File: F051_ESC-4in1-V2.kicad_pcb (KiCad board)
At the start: 4 copper layers, 46 x 55.8 mm, 222 parts, among them J1 Conn_01x02, J11 Conn_01x03, J14 Conn_01x03, J2 Conn_01x10, J3 Conn_01x05, J4 Conn_01x05, J5 Conn_01x05, J6 Conn_01x03, J7 Conn_01x05, J8 Conn_01x03, J9 Conn_01x10, Q1 TPHR8504PL, Q10 TPHR8504PL, Q11 TPHR8504PL, Q12 TPHR8504PL, Q13 TPHR8504PL, Q14 TPHR8504PL, Q15 TPHR8504PL, Q16 TPHR8504PL, Q17 TPHR8504PL, Q18 TPHR8504PL, Q19 TPHR8504PL, Q2 TPHR8504PL, Q20 TPHR8504PL, Q21 TPHR8504PL, Q22 TPHR8504PL, Q23 TPHR8504PL, Q24 TPHR8504PL, Q3 TPHR8504PL, Q4 TPHR8504PL, Q5 TPHR8504PL, Q6 TPHR8504PL, Q7 TPHR8504PL, Q8 TPHR8504PL, Q9 TPHR8504PL, U1 STM32F051K6Ux, U10 FD6288Q, U11 STM32F051K6Ux, U12 FD6288Q, U13 L78L12_SOT89, U14 MP4560_QFN10, U2 FD6288Q, U3 L78L12_SOT89, U4 LP2985-3.3, U5 INA139, U6 FD6288Q, U7 OPA340NA, U8 STM32F051K6Ux, U9 STM32F051K6Ux

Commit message: More routing
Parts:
- moved C17 54.9 mm to (132.9, 101.1)
- moved C20 54.9 mm to (132.9, 98.8)
- moved C50 54.9 mm to (132.9, 87.3)
- moved C52 54.9 mm to (132.9, 78.2)
- moved C53 54.9 mm to (132.9, 94.2)
- moved C54 54.9 mm to (132.9, 85.1)
- moved C55 54.9 mm to (132.9, 75.9)
- moved C56 54.9 mm to (132.9, 91.9)
- moved C57 54.9 mm to (132.9, 82.8)
- moved C59 54.9 mm to (132.9, 80.5)
- moved C61 54.9 mm to (132.9, 96.5)
- moved C63 54.9 mm to (132.9, 89.6)
- moved C16 28.6 mm to (147.1, 89.6)
- moved C18 28.6 mm to (147.1, 82.8)
- moved C19 28.6 mm to (147.1, 91.9)
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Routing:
- net Net-(Q4-Pad4): track 15.9 -> 0.00 mm
- net Net-(Q22-Pad4): track 15.1 -> 0.00 mm
- net /MCU 3/PhaseA: track 17.6 -> 2.95 mm, vias 30 -> 28
- net /MCU 4/PhaseC: track 19.6 -> 5.28 mm, vias 29 -> 27
- net /MCU 1/PhaseA: track 18.8 -> 5.94 mm, vias 29 -> 27
- net /MCU 3/PhaseB: track 15.5 -> 2.76 mm, vias 29 -> 27
- net Net-(Q16-Pad4): track 0.00 -> 11.2 mm
- net /MCU 1/PhaseB: track 15.1 -> 4.30 mm, vias 29 -> 27
- net Net-(Q14-Pad4): track 0.00 -> 10.6 mm
- net Net-(Q24-Pad4): track 9.34 -> 0.00 mm
- net /MOSFET Driver 3/HO1: track 8.67 -> 0.02 mm
- net /MOSFET Driver 3/HO2: track 7.22 -> 0.00 mm
- net /MCU 4/PhaseB: track 11.5 -> 4.43 mm, vias 29 -> 28
- net VCC_Shunt: track 6.57 -> 0.00 mm, vias 234 -> 107
- net /MOSFET Driver 3/VB2: track 7.54 -> 1.61 mm
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- added copper zone on F.Cu, net +5V
- added copper zone on F.Cu, net Net-(C70-Pad1)

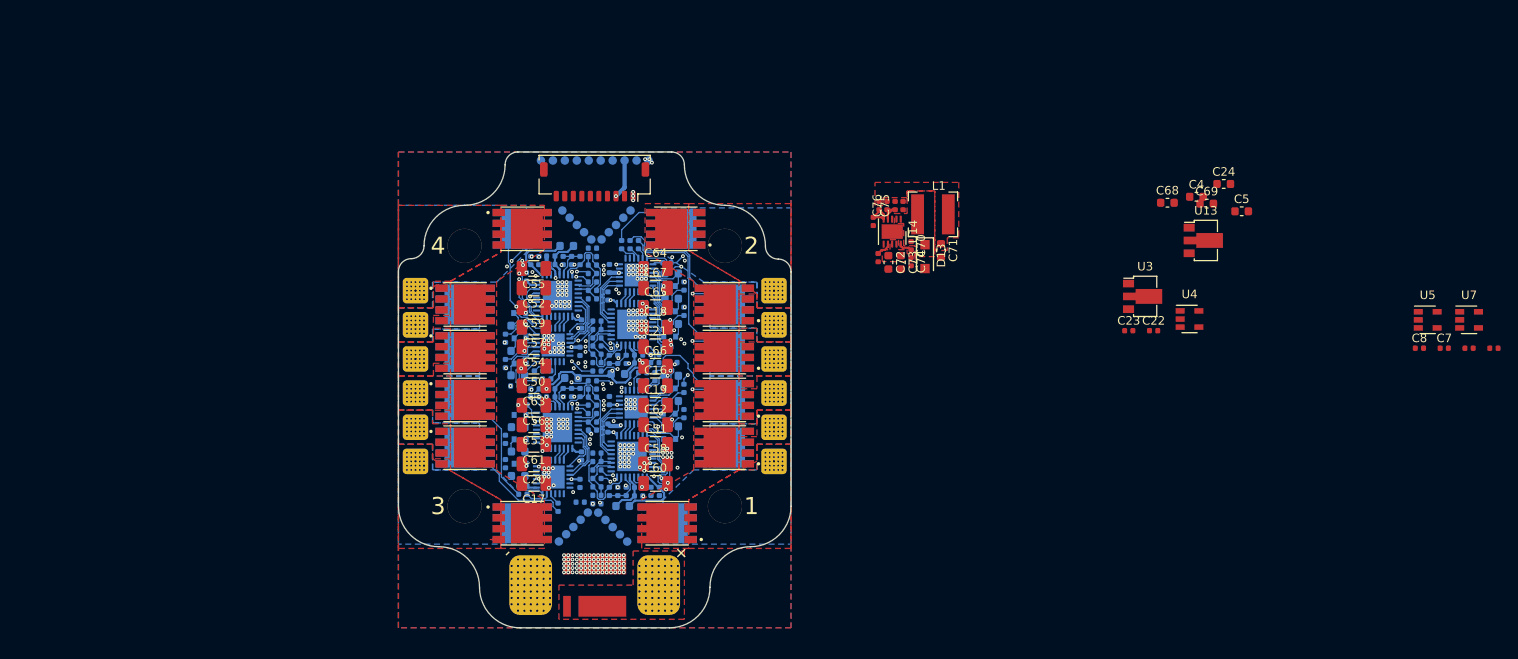
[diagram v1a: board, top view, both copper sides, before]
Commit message: Lots of changes made with back being rerouted
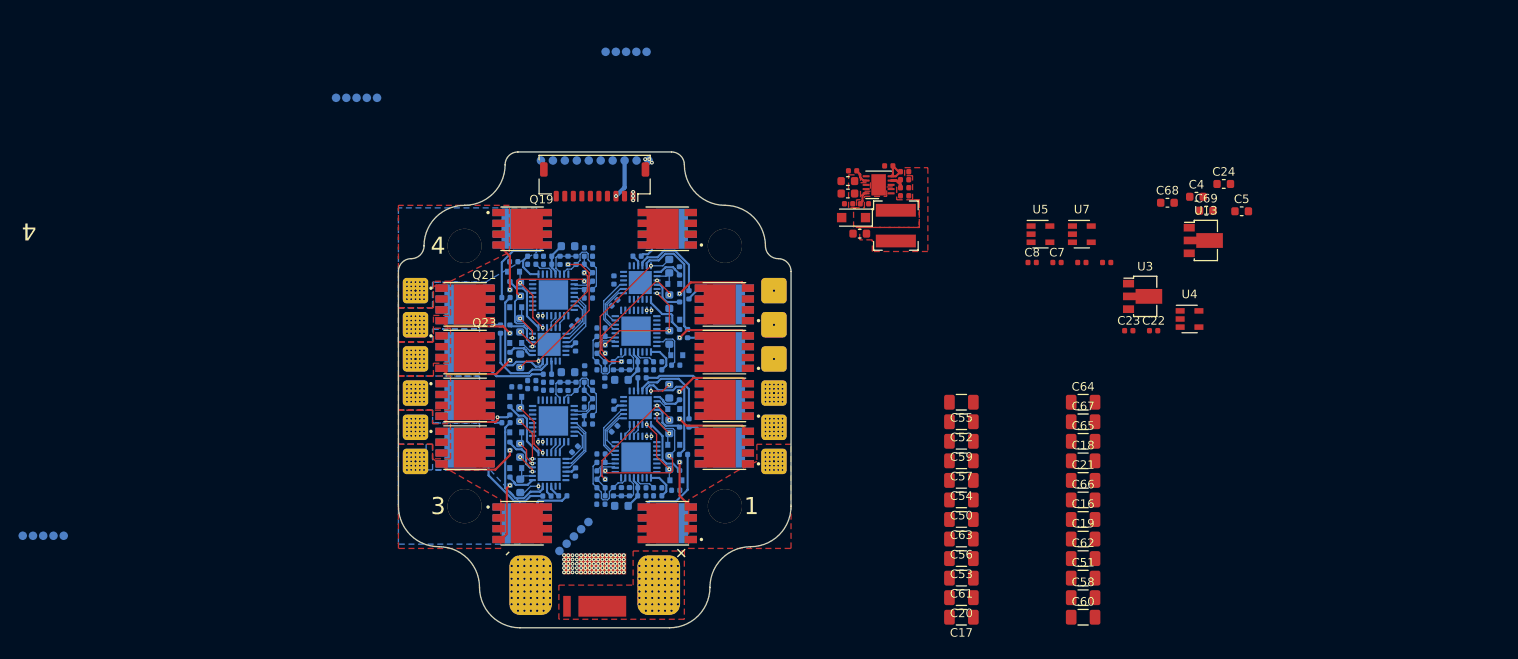
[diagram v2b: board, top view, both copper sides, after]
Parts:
- removed J14: Conn_01x03, Connector_Wire:Conn_MotorPhase
- added J10: Conn_01x03, Connector_Wire:Conn_MotorPhase, B.Cu at (119.0, 82.5)
- C1, C27, C41: value 10nF -> 0.1uF
- C10: value 0.1uF -> 1uF; footprint Capacitor_SMD:C_0603_1608Metric -> Capacitor_SMD:C_0402_1005Metric
- C11, C45, C9: value 0.1uF -> 10nF
- C12, C46: value 0.1uF -> 1uF
- C13, C14, C15, C25, C26, C47, C48, C49: footprint Capacitor_SMD:C_0603_1608Metric -> Capacitor_SMD:C_0402_1005Metric
- C2, C42: value 1uF -> 0.1uF; footprint Capacitor_SMD:C_0402_1005Metric -> Capacitor_SMD:C_0603_1608Metric
- C28: value 1uF -> 0.1uF
- C29, C3, C30, C31, C43, C44, C6: footprint Capacitor_SMD:C_0402_1005Metric -> Capacitor_SMD:C_0603_1608Metric
- J6, J8: moved to B.Cu
- Q1, Q10, Q11, Q12, Q13, Q14, Q15, Q16, Q17, Q18, Q19, Q2, Q20, Q21, Q22, Q23, Q24, Q3, Q4, Q5, Q6, Q7, Q8, Q9: value TPHR8504PL -> TPH1R204PB; footprint Footprints:TPHR8504PL -> Footprints:TPH1R204PB
- R10, R12, R32, R33, R55, R56, R57, R58, R60, R7, R8, R9: value 10k -> 10
- R11, R34, R35, R36, R37, R59: value 1k -> 10
- R14, R16, R17, R62, R63, R64: value 1k -> 10k
- R18, R19, R22, R26, R4, R5, R6, R66, R67: value 10 -> 10k
- R20, R21, R23, R24, R25, R68, R69, R70, R71: value 10 -> 1k
- R28, R29, R30: value 10k -> 1k
- U1, U11, U8: value STM32F051K6Ux -> FD6288Q; footprint Package_DFN_QFN:QFN-32-1EP_5x5mm_P0.5mm_EP3.45x3.45mm -> Package_DFN_QFN:QFN-24-1EP_4x4mm_P0.5mm_EP2.7x2.7mm
- U12, U2, U6: value FD6288Q -> STM32F051K6Ux; footprint Package_DFN_QFN:QFN-24-1EP_4x4mm_P0.5mm_EP2.7x2.7mm -> Package_DFN_QFN:QFN-32-1EP_5x5mm_P0.5mm_EP3.45x3.45mm
- moved J5 76.4 mm to (75.4, 107.2), turned to 0 degrees
- moved J3 55.7 mm to (143.7, 50.5), turned to 0 degrees
- moved C16 52.5 mm to (197.2, 105.3)
- moved C17 52.5 mm to (183.0, 116.8)
- moved C18 52.5 mm to (197.2, 98.4)
- moved C20 52.5 mm to (183.0, 114.5)
- moved C21 52.5 mm to (197.2, 100.7)
- moved C50 52.5 mm to (183.0, 103.0)
- moved C51 52.5 mm to (197.2, 112.2)
- moved C52 52.5 mm to (183.0, 93.9)
- moved C53 52.5 mm to (183.0, 109.9)
- moved C54 52.5 mm to (183.0, 100.7)
- moved C57 52.5 mm to (183.0, 98.4)
- moved C58 52.5 mm to (197.2, 114.5)
- moved C59 52.5 mm to (183.0, 96.2)
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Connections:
- C1 pad 1: +3.3VA_1 -> +12V_2
- C10 pad 1: /MOSFET Driver 2/VB1 -> +3.3VA_2
- C10 pad 2: /MCU 2/PhaseA -> GND
- C11 pad 1: /MCU 1/NRST -> +3.3VA_1
- C12 pad 1: +12V_2 -> +3.3VA_1
- C13 pad 1: /MOSFET Driver 1/VB1 -> +3V3
- C13 pad 2: /MCU 1/PhaseA -> GND
- C14 pad 1: /MOSFET Driver 1/VB2 -> +3V3
- C14 pad 2: /MCU 1/PhaseB -> GND
- C15 pad 1: /MOSFET Driver 1/VB3 -> /MCU_1/NRST
- C15 pad 2: /MCU 1/PhaseC -> GND
- C2 pad 1: +3.3VA_1 -> /MOSFET_Driver_1/VB1
- C2 pad 2: GND -> /MCU_1/PhaseA
- C25 pad 1: /MOSFET Driver 2/VB2 -> +3V3
- C25 pad 2: /MCU 2/PhaseB -> GND
- C26 pad 1: /MOSFET Driver 2/VB3 -> +3V3
- C26 pad 2: /MCU 2/PhaseC -> GND
- C27 pad 1: +3.3VA_2 -> /MCU_2/NRST
- C28 pad 1: +3.3VA_2 -> +12V_2
- C29 pad 1: +3V3 -> /MOSFET_Driver_2/VB1
- C29 pad 2: GND -> /MCU_2/PhaseA
- C3 pad 1: +3V3 -> /MOSFET_Driver_1/VB2
- C3 pad 2: GND -> /MCU_1/PhaseB
- C30 pad 1: +3V3 -> /MOSFET_Driver_2/VB2
- C30 pad 2: GND -> /MCU_2/PhaseB
- C31 pad 1: /MCU 2/NRST -> /MOSFET_Driver_2/VB3
- C31 pad 2: GND -> /MCU_2/PhaseC
- C41 pad 1: +3.3VA_4 -> +12V_1
- C42 pad 1: +3.3VA_4 -> /MOSFET_Driver_4/VB1
- C42 pad 2: GND -> /MCU_4/PhaseA
- C43 pad 1: +3V3 -> /MOSFET_Driver_4/VB2
- C43 pad 2: GND -> /MCU_4/PhaseB
- C44 pad 1: +3V3 -> /MOSFET_Driver_4/VB3
- C44 pad 2: GND -> /MCU_4/PhaseC
- C45 pad 1: /MCU 4/NRST -> +3.3VA_4
- C46 pad 1: +12V_1 -> +3.3VA_4
- C47 pad 1: /MOSFET Driver 4/VB1 -> +3V3
- C47 pad 2: /MCU 4/PhaseA -> GND
- C48 pad 1: /MOSFET Driver 4/VB2 -> +3V3
- C48 pad 2: /MCU 4/PhaseB -> GND
- C49 pad 1: /MOSFET Driver 4/VB3 -> /MCU_4/NRST
- C49 pad 2: /MCU 4/PhaseC -> GND
- C6 pad 1: +3V3 -> /MOSFET_Driver_1/VB3
- C6 pad 2: GND -> /MCU_1/PhaseC
- C9 pad 1: +12V_2 -> +3.3VA_2
- D1 pad 1: /MOSFET Driver 2/VB1 -> /MOSFET_Driver_2/VB1
- D10 pad 1: /MOSFET Driver 4/VB1 -> /MOSFET_Driver_4/VB1
- D11 pad 1: /MOSFET Driver 4/VB2 -> /MOSFET_Driver_4/VB2
- D12 pad 1: /MOSFET Driver 4/VB3 -> /MOSFET_Driver_4/VB3
- D2 pad 1: /MOSFET Driver 1/VB1 -> /MOSFET_Driver_1/VB1
- D3 pad 1: /MOSFET Driver 1/VB2 -> /MOSFET_Driver_1/VB2
- D4 pad 1: /MOSFET Driver 1/VB3 -> /MOSFET_Driver_1/VB3
- D5 pad 1: /MOSFET Driver 2/VB2 -> /MOSFET_Driver_2/VB2
- D6 pad 1: /MOSFET Driver 2/VB3 -> /MOSFET_Driver_2/VB3
- J3 pad 1: /MCU 1/SWCLK -> /MCU_1/SWCLK
- J3 pad 2: /MCU 1/SWDIO -> /MCU_1/SWDIO
- J3 pad 3: /MCU 1/NRST -> /MCU_1/NRST
- J3 pad 4: /MCU 1/USART1_RX -> /MCU_1/USART1_RX
- J3 pad 5: /MCU 1/USART1_TX -> /MCU_1/USART1_TX
- J5 pad 1: /MCU 2/SWCLK -> /MCU_2/SWCLK
- J5 pad 2: /MCU 2/SWDIO -> /MCU_2/SWDIO
- J5 pad 3: /MCU 2/NRST -> /MCU_2/NRST
- J5 pad 4: /MCU 2/USART1_RX -> /MCU_2/USART1_RX
- J5 pad 5: /MCU 2/USART1_TX -> /MCU_2/USART1_TX
- J6 pad 1: /MCU 1/PhaseC -> /MCU_1/PhaseC
- J6 pad 2: /MCU 1/PhaseB -> /MCU_1/PhaseB
- J6 pad 3: /MCU 1/PhaseA -> /MCU_1/PhaseA
- J7 pad 1: /MCU 4/SWCLK -> /MCU_4/SWCLK
- J7 pad 2: /MCU 4/SWDIO -> /MCU_4/SWDIO
- J7 pad 3: /MCU 4/NRST -> /MCU_4/NRST
- J7 pad 4: /MCU 4/USART1_RX -> /MCU_4/USART1_RX
- J7 pad 5: /MCU 4/USART1_TX -> /MCU_4/USART1_TX
- J8 pad 1: /MCU 2/PhaseC -> /MCU_2/PhaseC
- J8 pad 2: /MCU 2/PhaseB -> /MCU_2/PhaseB
- J8 pad 3: /MCU 2/PhaseA -> /MCU_2/PhaseA
- Q1 pad 1: /MCU 1/PhaseA -> /MCU_1/PhaseA
- Q1 pad 2: /MCU 1/PhaseA -> /MCU_1/PhaseA
- Q1 pad 3: /MCU 1/PhaseA -> /MCU_1/PhaseA
- Q10 pad 5: /MCU 2/PhaseB -> /MCU_2/PhaseB
- Q10 pad 6: /MCU 2/PhaseB -> /MCU_2/PhaseB
- Q10 pad 7: /MCU 2/PhaseB -> /MCU_2/PhaseB
- Q10 pad 8: /MCU 2/PhaseB -> /MCU_2/PhaseB
- Q10 pad 9: /MCU 2/PhaseB -> /MCU_2/PhaseB
- Q11 pad 1: /MCU 2/PhaseC -> /MCU_2/PhaseC
- Q11 pad 2: /MCU 2/PhaseC -> /MCU_2/PhaseC
- Q11 pad 3: /MCU 2/PhaseC -> /MCU_2/PhaseC
- Q12 pad 5: /MCU 2/PhaseC -> /MCU_2/PhaseC
- Q12 pad 6: /MCU 2/PhaseC -> /MCU_2/PhaseC
- Q12 pad 7: /MCU 2/PhaseC -> /MCU_2/PhaseC
- Q12 pad 8: /MCU 2/PhaseC -> /MCU_2/PhaseC
- Q12 pad 9: /MCU 2/PhaseC -> /MCU_2/PhaseC
- Q19 pad 1: /MCU 4/PhaseA -> /MCU_4/PhaseA
- Q19 pad 2: /MCU 4/PhaseA -> /MCU_4/PhaseA
- Q19 pad 3: /MCU 4/PhaseA -> /MCU_4/PhaseA
- Q2 pad 5: /MCU 1/PhaseA -> /MCU_1/PhaseA
- Q2 pad 6: /MCU 1/PhaseA -> /MCU_1/PhaseA
- Q2 pad 7: /MCU 1/PhaseA -> /MCU_1/PhaseA
- Q2 pad 8: /MCU 1/PhaseA -> /MCU_1/PhaseA
- Q2 pad 9: /MCU 1/PhaseA -> /MCU_1/PhaseA
- Q20 pad 5: /MCU 4/PhaseA -> /MCU_4/PhaseA
- Q20 pad 6: /MCU 4/PhaseA -> /MCU_4/PhaseA
- Q20 pad 7: /MCU 4/PhaseA -> /MCU_4/PhaseA
- Q20 pad 8: /MCU 4/PhaseA -> /MCU_4/PhaseA
- Q20 pad 9: /MCU 4/PhaseA -> /MCU_4/PhaseA
- Q21 pad 1: /MCU 4/PhaseB -> /MCU_4/PhaseB
- Q21 pad 2: /MCU 4/PhaseB -> /MCU_4/PhaseB
- Q21 pad 3: /MCU 4/PhaseB -> /MCU_4/PhaseB
- Q22 pad 5: /MCU 4/PhaseB -> /MCU_4/PhaseB
- Q22 pad 6: /MCU 4/PhaseB -> /MCU_4/PhaseB
- Q22 pad 7: /MCU 4/PhaseB -> /MCU_4/PhaseB
- Q22 pad 8: /MCU 4/PhaseB -> /MCU_4/PhaseB
- Q22 pad 9: /MCU 4/PhaseB -> /MCU_4/PhaseB
- Q23 pad 1: /MCU 4/PhaseC -> /MCU_4/PhaseC
- Q23 pad 2: /MCU 4/PhaseC -> /MCU_4/PhaseC
- Q23 pad 3: /MCU 4/PhaseC -> /MCU_4/PhaseC
- Q24 pad 5: /MCU 4/PhaseC -> /MCU_4/PhaseC
- Q24 pad 6: /MCU 4/PhaseC -> /MCU_4/PhaseC
- Q24 pad 7: /MCU 4/PhaseC -> /MCU_4/PhaseC
- Q24 pad 8: /MCU 4/PhaseC -> /MCU_4/PhaseC
- Q24 pad 9: /MCU 4/PhaseC -> /MCU_4/PhaseC
- Q3 pad 1: /MCU 1/PhaseB -> /MCU_1/PhaseB
- Q3 pad 2: /MCU 1/PhaseB -> /MCU_1/PhaseB
- Q3 pad 3: /MCU 1/PhaseB -> /MCU_1/PhaseB
- Q4 pad 5: /MCU 1/PhaseB -> /MCU_1/PhaseB
- Q4 pad 6: /MCU 1/PhaseB -> /MCU_1/PhaseB
- Q4 pad 7: /MCU 1/PhaseB -> /MCU_1/PhaseB
- Q4 pad 8: /MCU 1/PhaseB -> /MCU_1/PhaseB
- Q4 pad 9: /MCU 1/PhaseB -> /MCU_1/PhaseB
- Q5 pad 1: /MCU 1/PhaseC -> /MCU_1/PhaseC
- Q5 pad 2: /MCU 1/PhaseC -> /MCU_1/PhaseC
- Q5 pad 3: /MCU 1/PhaseC -> /MCU_1/PhaseC
- Q6 pad 5: /MCU 1/PhaseC -> /MCU_1/PhaseC
- Q6 pad 6: /MCU 1/PhaseC -> /MCU_1/PhaseC
- Q6 pad 7: /MCU 1/PhaseC -> /MCU_1/PhaseC
- Q6 pad 8: /MCU 1/PhaseC -> /MCU_1/PhaseC
- Q6 pad 9: /MCU 1/PhaseC -> /MCU_1/PhaseC
- Q7 pad 1: /MCU 2/PhaseA -> /MCU_2/PhaseA
- Q7 pad 2: /MCU 2/PhaseA -> /MCU_2/PhaseA
- Q7 pad 3: /MCU 2/PhaseA -> /MCU_2/PhaseA
- Q8 pad 5: /MCU 2/PhaseA -> /MCU_2/PhaseA
- Q8 pad 6: /MCU 2/PhaseA -> /MCU_2/PhaseA
- Q8 pad 7: /MCU 2/PhaseA -> /MCU_2/PhaseA
- Q8 pad 8: /MCU 2/PhaseA -> /MCU_2/PhaseA
- Q8 pad 9: /MCU 2/PhaseA -> /MCU_2/PhaseA
- Q9 pad 1: /MCU 2/PhaseB -> /MCU_2/PhaseB
- Q9 pad 2: /MCU 2/PhaseB -> /MCU_2/PhaseB
- Q9 pad 3: /MCU 2/PhaseB -> /MCU_2/PhaseB
- R10 pad 1: /MCU 1/SenseB -> Net-(Q4-Pad4)
- R10 pad 2: /MCU 1/SenseCOM -> /MOSFET_Driver_1/LO2
- R11 pad 1: Net-(R11-Pad1) -> Net-(Q5-Pad4)
- R11 pad 2: /PWM_1 -> /MOSFET_Driver_1/HO3
- R12 pad 1: /MCU 1/SenseC -> Net-(Q6-Pad4)
- R12 pad 2: /MCU 1/PhaseC -> /MOSFET_Driver_1/LO3
- R13 pad 1: /MCU 1/SenseC -> /MCU_1/SenseA
- R13 pad 2: /MCU 1/SenseCOM -> /MCU_1/PhaseA
- R14 pad 1: GND -> /MCU_1/SenseA
- R14 pad 2: /MCU 1/SenseA -> /MCU_1/SenseCOM
- R15 pad 1: GND -> Net-(R15-Pad1)
- R15 pad 2: /MCU 1/SenseB -> /PWM_1
- R16 pad 1: GND -> /MCU_1/SenseB
- R16 pad 2: /MCU 1/SenseC -> /MCU_1/PhaseB
- R17 pad 1: /MCU 1/BOOT0 -> /MCU_1/SenseB
- R17 pad 2: GND -> /MCU_1/SenseCOM
- R18 pad 1: Net-(Q1-Pad4) -> /MCU_1/SenseC
- R18 pad 2: /MOSFET Driver 1/HO1 -> /MCU_1/PhaseC
- R19 pad 1: Net-(Q2-Pad4) -> /MCU_1/SenseC
- R19 pad 2: /MOSFET Driver 1/LO1 -> /MCU_1/SenseCOM
- R20 pad 1: Net-(Q3-Pad4) -> GND
- R20 pad 2: /MOSFET Driver 1/HO2 -> /MCU_1/SenseA
- R21 pad 1: Net-(Q4-Pad4) -> GND
- R21 pad 2: /MOSFET Driver 1/LO2 -> /MCU_1/SenseB
- R22 pad 1: Net-(Q10-Pad4) -> /MCU_2/SenseB
- R22 pad 2: /MOSFET Driver 2/LO2 -> /MCU_2/SenseCOM
- R23 pad 1: Net-(Q5-Pad4) -> GND
- R23 pad 2: /MOSFET Driver 1/HO3 -> /MCU_1/SenseC
- R24 pad 1: Net-(Q6-Pad4) -> /MCU_1/BOOT0
- R24 pad 2: /MOSFET Driver 1/LO3 -> GND
- R25 pad 1: Net-(Q11-Pad4) -> Net-(R25-Pad1)
- R25 pad 2: /MOSFET Driver 2/HO3 -> /PWM_2
- R26 pad 1: Net-(Q12-Pad4) -> /MCU_2/SenseC
- R26 pad 2: /MOSFET Driver 2/LO3 -> /MCU_2/PhaseC
- R27 pad 1: /MCU 2/SenseA -> /MCU_2/SenseC
- R27 pad 2: /MCU 2/PhaseA -> /MCU_2/SenseCOM
- R28 pad 1: /MCU 2/SenseA -> GND
- R28 pad 2: /MCU 2/SenseCOM -> /MCU_2/SenseA
- R29 pad 1: /MCU 2/SenseB -> GND
- R29 pad 2: /MCU 2/PhaseB -> /MCU_2/SenseB
- R30 pad 1: /MCU 2/SenseB -> GND
- R30 pad 2: /MCU 2/SenseCOM -> /MCU_2/SenseC
- R31 pad 1: Net-(R31-Pad1) -> /MCU_2/BOOT0
- R31 pad 2: /PWM_2 -> GND
- R32 pad 1: /MCU 2/SenseC -> Net-(Q7-Pad4)
- R32 pad 2: /MCU 2/PhaseC -> /MOSFET_Driver_2/HO1
- R33 pad 1: /MCU 2/SenseC -> Net-(Q8-Pad4)
- R33 pad 2: /MCU 2/SenseCOM -> /MOSFET_Driver_2/LO1
- R34 pad 1: GND -> Net-(Q9-Pad4)
- R34 pad 2: /MCU 2/SenseA -> /MOSFET_Driver_2/HO2
- R35 pad 1: GND -> Net-(Q10-Pad4)
- R35 pad 2: /MCU 2/SenseB -> /MOSFET_Driver_2/LO2
- R36 pad 1: GND -> Net-(Q11-Pad4)
- R36 pad 2: /MCU 2/SenseC -> /MOSFET_Driver_2/HO3
- R37 pad 1: /MCU 2/BOOT0 -> Net-(Q12-Pad4)
- R37 pad 2: GND -> /MOSFET_Driver_2/LO3
- R4 pad 1: Net-(Q7-Pad4) -> /MCU_2/SenseA
- R4 pad 2: /MOSFET Driver 2/HO1 -> /MCU_2/PhaseA
- R5 pad 1: Net-(Q8-Pad4) -> /MCU_2/SenseA
- R5 pad 2: /MOSFET Driver 2/LO1 -> /MCU_2/SenseCOM
- R55 pad 1: /MCU 4/SenseA -> Net-(Q19-Pad4)
- R55 pad 2: /MCU 4/PhaseA -> /MOSFET_Driver_4/HO1
- R56 pad 1: /MCU 4/SenseA -> Net-(Q20-Pad4)
- R56 pad 2: /MCU 4/SenseCOM -> /MOSFET_Driver_4/LO1
- R57 pad 1: /MCU 4/SenseB -> Net-(Q21-Pad4)
- R57 pad 2: /MCU 4/PhaseB -> /MOSFET_Driver_4/HO2
- R58 pad 1: /MCU 4/SenseB -> Net-(Q22-Pad4)
- R58 pad 2: /MCU 4/SenseCOM -> /MOSFET_Driver_4/LO2
- R59 pad 1: Net-(R59-Pad1) -> Net-(Q23-Pad4)
- R59 pad 2: /PWM_4 -> /MOSFET_Driver_4/HO3
- R6 pad 1: Net-(Q9-Pad4) -> /MCU_2/SenseB
- R6 pad 2: /MOSFET Driver 2/HO2 -> /MCU_2/PhaseB
- R60 pad 1: /MCU 4/SenseC -> Net-(Q24-Pad4)
- R60 pad 2: /MCU 4/PhaseC -> /MOSFET_Driver_4/LO3
- R61 pad 1: /MCU 4/SenseC -> /MCU_4/SenseA
- R61 pad 2: /MCU 4/SenseCOM -> /MCU_4/PhaseA
- R62 pad 1: GND -> /MCU_4/SenseA
- R62 pad 2: /MCU 4/SenseA -> /MCU_4/SenseCOM
- R63 pad 1: GND -> /MCU_4/SenseB
- R63 pad 2: /MCU 4/SenseB -> /MCU_4/PhaseB
- R64 pad 1: GND -> /MCU_4/SenseB
- R64 pad 2: /MCU 4/SenseC -> /MCU_4/SenseCOM
- R65 pad 1: /MCU 4/BOOT0 -> Net-(R65-Pad1)
- R65 pad 2: GND -> /PWM_4
- R66 pad 1: Net-(Q19-Pad4) -> /MCU_4/SenseC
- R66 pad 2: /MOSFET Driver 4/HO1 -> /MCU_4/PhaseC
- R67 pad 1: Net-(Q20-Pad4) -> /MCU_4/SenseC
- R67 pad 2: /MOSFET Driver 4/LO1 -> /MCU_4/SenseCOM
- R68 pad 1: Net-(Q21-Pad4) -> GND
- R68 pad 2: /MOSFET Driver 4/HO2 -> /MCU_4/SenseA
- R69 pad 1: Net-(Q22-Pad4) -> GND
- R69 pad 2: /MOSFET Driver 4/LO2 -> /MCU_4/SenseB
- R7 pad 1: /MCU 1/SenseA -> Net-(Q1-Pad4)
- R7 pad 2: /MCU 1/PhaseA -> /MOSFET_Driver_1/HO1
- R70 pad 1: Net-(Q23-Pad4) -> GND
- R70 pad 2: /MOSFET Driver 4/HO3 -> /MCU_4/SenseC
- R71 pad 1: Net-(Q24-Pad4) -> /MCU_4/BOOT0
- R71 pad 2: /MOSFET Driver 4/LO3 -> GND
- R8 pad 1: /MCU 1/SenseA -> Net-(Q2-Pad4)
- R8 pad 2: /MCU 1/SenseCOM -> /MOSFET_Driver_1/LO1
- R9 pad 1: /MCU 1/SenseB -> Net-(Q3-Pad4)
- R9 pad 2: /MCU 1/PhaseB -> /MOSFET_Driver_1/HO2
- U1 pad 1: +3V3 -> /MCU_1/LIN1
- U1 pad 10: /MCU 1/SenseB -> /MOSFET_Driver_1/LO2
- U1 pad 11: /MCU 1/SenseA -> /MOSFET_Driver_1/LO1
- U1 pad 12: (no net) -> /MCU_1/PhaseC
- U1 pad 13: /MCU 1/LIN3 -> /MOSFET_Driver_1/HO3
- U1 pad 14: /MCU 1/LIN2 -> /MOSFET_Driver_1/VB3
- U1 pad 15: /MCU 1/LIN1 -> /MCU_1/PhaseB
- U1 pad 16: (no net) -> /MOSFET_Driver_1/HO2
- U1 pad 17: +3V3 -> /MOSFET_Driver_1/VB2
- U1 pad 18: /MCU 1/HIN1 -> /MCU_1/PhaseA
- U1 pad 19: /MCU 1/HIN2 -> /MOSFET_Driver_1/HO1
- U1 pad 2: (no net) -> /MCU_1/LIN2
- U1 pad 20: /MOSFET Driver 1/HIN1 -> /MOSFET_Driver_1/VB1
- U1 pad 22: (no net) -> /MOSFET_Driver_1/HIN1
- U1 pad 23: /MCU 1/SWDIO -> /MCU_1/HIN2
- U1 pad 24: /MCU 1/SWCLK -> /MCU_1/HIN1
- U1 pad 25: (no net) -> GND
- U1 pad 3: (no net) -> /MCU_1/LIN3
- U1 pad 4: /MCU 1/NRST -> +12V_2
- U1 pad 5: +3.3VA_1 -> (no net)
- U1 pad 6: /MCU 1/SenseC -> GND
- U1 pad 7: /MCU 1/SenseCOM -> (no net)
- U1 pad 8: Net-(R11-Pad1) -> (no net)
- U1 pad 9: (no net) -> /MOSFET_Driver_1/LO3
- U11 pad 1: +3V3 -> /MCU_4/LIN1
- U11 pad 10: /MCU 4/SenseB -> /MOSFET_Driver_4/LO2
- U11 pad 11: /MCU 4/SenseA -> /MOSFET_Driver_4/LO1
- U11 pad 12: (no net) -> /MCU_4/PhaseC
- U11 pad 13: /MCU 4/LIN3 -> /MOSFET_Driver_4/HO3
- U11 pad 14: /MCU 4/LIN2 -> /MOSFET_Driver_4/VB3
- U11 pad 15: /MCU 4/LIN1 -> /MCU_4/PhaseB
- U11 pad 16: (no net) -> /MOSFET_Driver_4/HO2
- U11 pad 17: +3V3 -> /MOSFET_Driver_4/VB2
- U11 pad 18: /MCU 4/HIN1 -> /MCU_4/PhaseA
- U11 pad 19: /MCU 4/HIN2 -> /MOSFET_Driver_4/HO1
- U11 pad 2: (no net) -> /MCU_4/LIN2
- U11 pad 20: /MOSFET Driver 4/HIN1 -> /MOSFET_Driver_4/VB1
- U11 pad 22: (no net) -> /MOSFET_Driver_4/HIN1
- U11 pad 23: /MCU 4/SWDIO -> /MCU_4/HIN2
- U11 pad 24: /MCU 4/SWCLK -> /MCU_4/HIN1
- U11 pad 25: (no net) -> GND
- U11 pad 3: (no net) -> /MCU_4/LIN3
- U11 pad 4: /MCU 4/NRST -> +12V_1
- U11 pad 5: +3.3VA_4 -> (no net)
- U11 pad 6: /MCU 4/SenseC -> GND
- U11 pad 7: /MCU 4/SenseCOM -> (no net)
- U11 pad 8: Net-(R59-Pad1) -> (no net)
- U11 pad 9: (no net) -> /MOSFET_Driver_4/LO3
- U12 pad 1: /MCU 4/LIN1 -> +3V3
- U12 pad 10: /MOSFET Driver 4/LO2 -> /MCU_4/SenseB
- U12 pad 11: /MOSFET Driver 4/LO1 -> /MCU_4/SenseA
- U12 pad 12: /MCU 4/PhaseC -> (no net)
- U12 pad 13: /MOSFET Driver 4/HO3 -> /MCU_4/LIN3
- U12 pad 14: /MOSFET Driver 4/VB3 -> /MCU_4/LIN2
- U12 pad 15: /MCU 4/PhaseB -> /MCU_4/LIN1
- U12 pad 16: /MOSFET Driver 4/HO2 -> (no net)
- U12 pad 17: /MOSFET Driver 4/VB2 -> +3V3
- U12 pad 18: /MCU 4/PhaseA -> /MCU_4/HIN1
- U12 pad 19: /MOSFET Driver 4/HO1 -> /MCU_4/HIN2
- U12 pad 2: /MCU 4/LIN2 -> (no net)
- U12 pad 20: /MOSFET Driver 4/VB1 -> /MOSFET_Driver_4/HIN1
- U12 pad 22: /MOSFET Driver 4/HIN1 -> (no net)
- U12 pad 23: /MCU 4/HIN2 -> /MCU_4/SWDIO
- U12 pad 24: /MCU 4/HIN1 -> /MCU_4/SWCLK
- U12 pad 25: GND -> (no net)
- U12 pad 3: /MCU 4/LIN3 -> (no net)
- U12 pad 4: +12V_1 -> /MCU_4/NRST
- U12 pad 5: (no net) -> +3.3VA_4
- U12 pad 6: GND -> /MCU_4/SenseC
- U12 pad 7: (no net) -> /MCU_4/SenseCOM
- U12 pad 8: (no net) -> Net-(R65-Pad1)
- U12 pad 9: /MOSFET Driver 4/LO3 -> (no net)
- U2 pad 1: /MCU 1/LIN1 -> +3V3
- U2 pad 10: /MOSFET Driver 1/LO2 -> /MCU_1/SenseB
- U2 pad 11: /MOSFET Driver 1/LO1 -> /MCU_1/SenseA
- U2 pad 12: /MCU 1/PhaseC -> (no net)
- U2 pad 13: /MOSFET Driver 1/HO3 -> /MCU_1/LIN3
- U2 pad 14: /MOSFET Driver 1/VB3 -> /MCU_1/LIN2
- U2 pad 15: /MCU 1/PhaseB -> /MCU_1/LIN1
- U2 pad 16: /MOSFET Driver 1/HO2 -> (no net)
- U2 pad 17: /MOSFET Driver 1/VB2 -> +3V3
- U2 pad 18: /MCU 1/PhaseA -> /MCU_1/HIN1
- U2 pad 19: /MOSFET Driver 1/HO1 -> /MCU_1/HIN2
- U2 pad 2: /MCU 1/LIN2 -> (no net)
- U2 pad 20: /MOSFET Driver 1/VB1 -> /MOSFET_Driver_1/HIN1
- U2 pad 22: /MOSFET Driver 1/HIN1 -> (no net)
- U2 pad 23: /MCU 1/HIN2 -> /MCU_1/SWDIO
- U2 pad 24: /MCU 1/HIN1 -> /MCU_1/SWCLK
- U2 pad 25: GND -> (no net)
- U2 pad 3: /MCU 1/LIN3 -> (no net)
- U2 pad 4: +12V_2 -> /MCU_1/NRST
- U2 pad 5: (no net) -> +3.3VA_1
- U2 pad 6: GND -> /MCU_1/SenseC
- U2 pad 7: (no net) -> /MCU_1/SenseCOM
- U2 pad 8: (no net) -> Net-(R15-Pad1)
- U2 pad 9: /MOSFET Driver 1/LO3 -> (no net)
- U6 pad 1: /MCU 2/LIN1 -> +3V3
- U6 pad 10: /MOSFET Driver 2/LO2 -> /MCU_2/SenseB
- U6 pad 11: /MOSFET Driver 2/LO1 -> /MCU_2/SenseA
- U6 pad 12: /MCU 2/PhaseC -> (no net)
- U6 pad 13: /MOSFET Driver 2/HO3 -> /MCU_2/LIN3
- U6 pad 14: /MOSFET Driver 2/VB3 -> /MCU_2/LIN2
- U6 pad 15: /MCU 2/PhaseB -> /MCU_2/LIN1
- U6 pad 16: /MOSFET Driver 2/HO2 -> (no net)
- U6 pad 17: /MOSFET Driver 2/VB2 -> +3V3
- U6 pad 18: /MCU 2/PhaseA -> /MCU_2/HIN1
- U6 pad 19: /MOSFET Driver 2/HO1 -> /MCU_2/HIN2
- U6 pad 2: /MCU 2/LIN2 -> (no net)
- U6 pad 20: /MOSFET Driver 2/VB1 -> /MOSFET_Driver_2/HIN1
- U6 pad 22: /MOSFET Driver 2/HIN1 -> (no net)
- U6 pad 23: /MCU 2/HIN2 -> /MCU_2/SWDIO
- U6 pad 24: /MCU 2/HIN1 -> /MCU_2/SWCLK
- U6 pad 25: GND -> (no net)
- U6 pad 3: /MCU 2/LIN3 -> (no net)
- U6 pad 4: +12V_2 -> /MCU_2/NRST
- U6 pad 5: (no net) -> +3.3VA_2
- U6 pad 6: GND -> /MCU_2/SenseC
- U6 pad 7: (no net) -> /MCU_2/SenseCOM
- U6 pad 8: (no net) -> Net-(R25-Pad1)
- U6 pad 9: /MOSFET Driver 2/LO3 -> (no net)
- U8 pad 1: +3V3 -> /MCU_2/LIN1
- U8 pad 10: /MCU 2/SenseB -> /MOSFET_Driver_2/LO2
- U8 pad 11: /MCU 2/SenseA -> /MOSFET_Driver_2/LO1
- U8 pad 12: (no net) -> /MCU_2/PhaseC
- U8 pad 13: /MCU 2/LIN3 -> /MOSFET_Driver_2/HO3
- U8 pad 14: /MCU 2/LIN2 -> /MOSFET_Driver_2/VB3
- U8 pad 15: /MCU 2/LIN1 -> /MCU_2/PhaseB
- U8 pad 16: (no net) -> /MOSFET_Driver_2/HO2
- U8 pad 17: +3V3 -> /MOSFET_Driver_2/VB2
- U8 pad 18: /MCU 2/HIN1 -> /MCU_2/PhaseA
- U8 pad 19: /MCU 2/HIN2 -> /MOSFET_Driver_2/HO1
- U8 pad 2: (no net) -> /MCU_2/LIN2
- U8 pad 20: /MOSFET Driver 2/HIN1 -> /MOSFET_Driver_2/VB1
- U8 pad 22: (no net) -> /MOSFET_Driver_2/HIN1
- U8 pad 23: /MCU 2/SWDIO -> /MCU_2/HIN2
- U8 pad 24: /MCU 2/SWCLK -> /MCU_2/HIN1
- U8 pad 25: (no net) -> GND
- U8 pad 3: (no net) -> /MCU_2/LIN3
- U8 pad 4: /MCU 2/NRST -> +12V_2
- U8 pad 5: +3.3VA_2 -> (no net)
- U8 pad 6: /MCU 2/SenseC -> GND
- U8 pad 7: /MCU 2/SenseCOM -> (no net)
- U8 pad 8: Net-(R31-Pad1) -> (no net)
- U8 pad 9: (no net) -> /MOSFET_Driver_2/LO3
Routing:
- net +3V3: track 44.9 -> 10.9 mm, vias 8 -> 0
- net /MCU_4/PhaseA: track 0.00 -> 25.7 mm, vias 0 -> 28
- net /MCU 4/PhaseA: track 20.6 -> 0.96 mm, vias 30 -> 0
- net /MCU_4/PhaseC: track 0.00 -> 19.5 mm, vias 0 -> 28
- net /MCU_2/PhaseC: track 0.00 -> 18.0 mm, vias 0 -> 2
- net /MCU 2/PhaseB: track 17.9 -> 0.00 mm, vias 29 -> 0
- net /MCU_1/PhaseA: track 0.00 -> 17.4 mm, vias 0 -> 27
- net Net-(Q8-Pad4): track 16.9 -> 1.65 mm
- net /MCU_4/PhaseB: track 0.00 -> 15.2 mm, vias 0 -> 28
- net /MCU_1/PhaseB: track 0.00 -> 15.2 mm, vias 0 -> 28
- net /MCU 2/PhaseA: track 17.9 -> 3.67 mm, vias 29 -> 0
- net /MCU_2/PhaseB: track 0.00 -> 13.7 mm, vias 0 -> 3
- net /MOSFET_Driver_2/LO1: track 0.00 -> 13.5 mm
- net /MOSFET_Driver_4/LO1: track 0.00 -> 13.3 mm
- net /MOSFET_Driver_1/LO1: track 0.00 -> 13.3 mm
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- added copper zone on B.Cu, net /MCU_4/PhaseC
- removed copper zone on In2.Cu, net +12V_1
- removed copper zone on In2.Cu, net +12V_2
- removed copper zone on In2.Cu, net +3V3
- removed copper zone on B.Cu, net /MCU 1/PhaseA
- removed copper zone on B.Cu, net /MCU 1/PhaseB
- removed copper zone on F.Cu, net /MCU 1/PhaseB
- removed copper zone on B.Cu, net /MCU 1/PhaseC
- removed copper zone on F.Cu, net /MCU 1/PhaseC
- removed copper zone on B.Cu, net /MCU 2/PhaseA
- removed copper zone on F.Cu, net /MCU 2/PhaseA
- removed copper zone on B.Cu, net /MCU 2/PhaseB
- removed copper zone on F.Cu, net /MCU 2/PhaseB
- removed copper zone on B.Cu, net /MCU 2/PhaseC
- removed copper zone on F.Cu, net /MCU 2/PhaseC
- removed copper zone on B.Cu, net /MCU 4/PhaseC
- removed copper zone on B.Cu, net GND
- removed copper zone on F.Cu, net GND
- removed copper zone on In1.Cu, net GND
- removed copper zone on In2.Cu, net VCC_Shunt
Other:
- outline, holes or cut-outs redrawn

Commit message: Started adding filtering caps
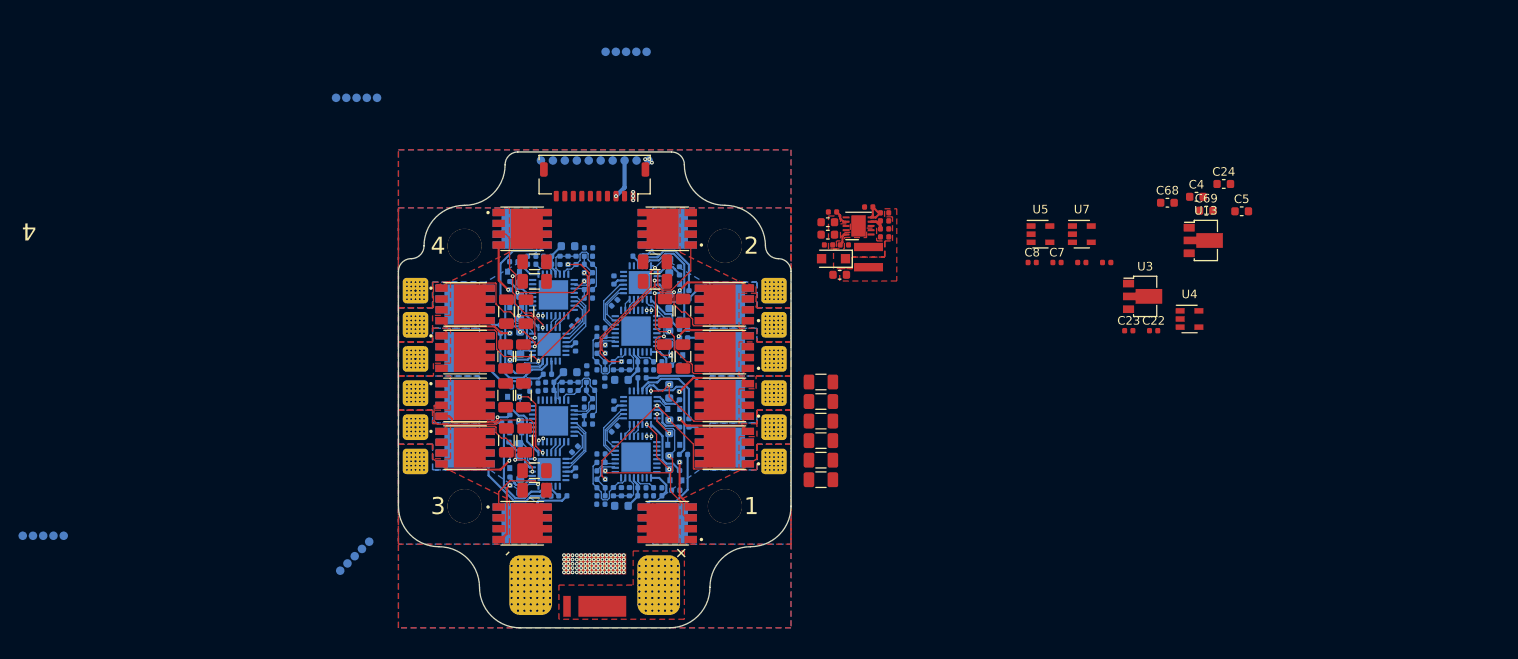
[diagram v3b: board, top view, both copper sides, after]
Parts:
- L1: value L_Small -> 12uH; footprint Inductor_SMD:L_Bourns-SRN5020 -> Inductor_SMD:L_XGL4030
- moved C67 67.6 mm to (129.7, 96.0), turned to 270 degrees
- moved C64 65.6 mm to (131.8, 96.0), turned to 270 degrees
- moved C57 56.1 mm to (129.7, 81.0), turned to 90 degrees
- moved C56 56.0 mm to (129.6, 90.8), turned to 90 degrees
- moved C54 55.3 mm to (129.6, 86.2), turned to 270 degrees
- moved C17 55.0 mm to (147.1, 75.1), turned to 0 degrees
- moved C50 54.0 mm to (131.7, 86.2), turned to 270 degrees
- moved C63 53.3 mm to (131.7, 90.8), turned to 90 degrees
- moved C59 53.2 mm to (131.9, 81.0), turned to 90 degrees
- moved C52 52.6 mm to (132.9, 77.4)
- moved C55 52.6 mm to (132.9, 75.1)
- moved C66 51.9 mm to (148.2, 86.2), turned to 270 degrees
- moved C20 51.6 mm to (147.1, 77.4), turned to 0 degrees
- moved C65 51.3 mm to (148.2, 80.9), turned to 90 degrees
- moved C53 51.1 mm to (132.9, 99.6)
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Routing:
- net /MCU_4/PhaseC: track 19.5 -> 33.9 mm, vias 28 -> 27
- net /MCU_4/PhaseB: track 15.2 -> 29.4 mm
- net /MCU 3/PhaseA: track 6.41 -> 20.5 mm
- net /MCU_2/PhaseB: track 13.7 -> 27.2 mm, vias 3 -> 28
- net /MCU_1/PhaseB: track 15.2 -> 28.0 mm
- net /MCU 3/PhaseB: track 3.71 -> 16.0 mm
- net /MCU_1/PhaseC: track 3.87 -> 15.2 mm
- net /MCU_2/PhaseC: track 18.0 -> 29.2 mm, vias 2 -> 27
- net /MOSFET_Driver_2/VB1: track 1.36 -> 11.1 mm, vias 0 -> 2
- net Net-(Q23-Pad4): track 8.98 -> 0.00 mm
- net /MCU 3/PhaseC: track 3.86 -> 11.0 mm
- net /MCU_2/PhaseA: track 13.2 -> 19.6 mm, vias 3 -> 28
- net /MCU_1/PhaseA: track 17.4 -> 23.3 mm
- net +3.3VA_3: track 0.00 -> 3.82 mm
- net /MCU 2/PhaseA: track 3.67 -> 0.00 mm
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- added copper zone on B.Cu, net /MCU_1/PhaseA
- added copper zone on F.Cu, net /MCU_1/PhaseA
- added copper zone on B.Cu, net /MCU_1/PhaseB
- added copper zone on F.Cu, net /MCU_1/PhaseB
- added copper zone on B.Cu, net /MCU_1/PhaseC
- added copper zone on F.Cu, net /MCU_1/PhaseC
- added copper zone on B.Cu, net /MCU_2/PhaseA
- added copper zone on F.Cu, net /MCU_2/PhaseA
- added copper zone on B.Cu, net /MCU_2/PhaseB
- added copper zone on F.Cu, net /MCU_2/PhaseB
- added copper zone on B.Cu, net /MCU_2/PhaseC
- added copper zone on F.Cu, net /MCU_2/PhaseC
- added copper zone on B.Cu, net /MCU_4/PhaseA
- added copper zone on F.Cu, net /MCU_4/PhaseA
- added copper zone on B.Cu, net /MCU_4/PhaseB
- added copper zone on F.Cu, net /MCU_4/PhaseB
- added copper zone on F.Cu, net /MCU_4/PhaseC
- added copper zone on B.Cu, net GND
- added copper zone on F.Cu, net GND
- added copper zone on In1.Cu, net GND
- added copper zone on In2.Cu, net VCC_Shunt
- removed copper zone on F.Cu, net /MCU 1/PhaseA
- removed copper zone on B.Cu, net /MCU 4/PhaseA
- removed copper zone on F.Cu, net /MCU 4/PhaseA
- removed copper zone on B.Cu, net /MCU 4/PhaseB
- removed copper zone on F.Cu, net /MCU 4/PhaseB
- removed copper zone on F.Cu, net /MCU 4/PhaseC

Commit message: More routing done
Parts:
- added G***: LOGO, Footprints:DTOM_L, F.Cu at (172.6, 84.8)
- U13, U3: footprint Package_TO_SOT_SMD:SOT-89-3 -> Footprints:L78L12ACUTR
- moved C69 79.9 mm to (136.7, 96.8)
- moved C68 78.7 mm to (136.7, 103.3)
- moved U13 78.4 mm to (137.9, 100.1), turned to 270 degrees
- moved C5 77.9 mm to (143.3, 97.8)
- moved C4 76.6 mm to (139.7, 96.8), turned to 180 degrees
- moved C24 71.1 mm to (143.9, 79.8), turned to 90 degrees
- moved U4 68.4 mm to (141.4, 79.3), turned to 270 degrees
- moved C22 66.5 mm to (139.1, 79.3), turned to 270 degrees
- moved U3 65.6 mm to (142.5, 101.5), turned to 180 degrees
- moved U7 65.5 mm to (141.8, 107.0), turned to 180 degrees
- moved R2 65.0 mm to (139.1, 104.5), turned to 180 degrees
- moved U5 64.5 mm to (138.1, 106.9), turned to 270 degrees
- moved R3 64.4 mm to (142.8, 104.7)
- moved C7 64.1 mm to (137.2, 104.5), turned to 180 degrees
- moved C8 58.3 mm to (140.9, 104.7)
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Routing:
- net +12V_2: track 2.62 -> 30.4 mm, vias 0 -> 8
- net /MCU_1/PhaseC: track 15.2 -> 39.1 mm
- net +12V_1: track 2.62 -> 19.7 mm, vias 0 -> 8
- net /MCU_1/PhaseA: track 23.3 -> 34.7 mm
- net /MCU_2/PhaseB: track 27.2 -> 16.1 mm
- net Net-(Q23-Pad4): track 0.00 -> 9.94 mm
- net Net-(Q11-Pad4): track 0.00 -> 7.76 mm, vias 0 -> 1
- net /MOSFET_Driver_2/VB2: track 0.00 -> 5.69 mm, vias 0 -> 2
- net VCC: track 0.00 -> 4.77 mm
- net /MOSFET_Driver_1/VB1: track 7.68 -> 12.4 mm
- net Net-(R2-Pad1): track 0.00 -> 4.63 mm
- net /MCU_2/PhaseA: track 19.6 -> 24.1 mm
- net /MCU_2/PhaseC: track 29.2 -> 24.7 mm
- net Net-(R3-Pad2): track 0.00 -> 4.36 mm
- net /MCU_1/BOOT0: track 0.00 -> 4.19 mm
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- added copper zone on In2.Cu, net +12V_1
- added copper zone on In2.Cu, net +12V_2
